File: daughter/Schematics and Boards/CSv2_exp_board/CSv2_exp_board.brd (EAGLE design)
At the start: 38.1 x 43.8 mm, 133 parts, among them J1 HIROSE-DF40_44-PIN_CONNECTORS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, J2 J-SERIAL-PORT, J3 CORTEX_DEBUG_SMD, J301 HIROSE-DF40_44-PIN_CONNECTORS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, J4 SJ-43514-SMT, J7 J-USB-HIROSE-MICRO-USB, SW1 SPST_TACT-KMR2, SW2 SPST_TACT-KMR2, U1 LOADSWITCH-MIC94164, U10 LOADSWITCH-MIC94164, U11 BMI160, U12 TLV320DAC26IRHB, U13 ADG839YKSZ-500RL7KS_6_ADI-L, U14 LOADSWITCH-MIC94164, U2 ADA4841-1YRJZ-R7, U205 MPL3115A2, U3 Value, U4 RFM69HCW, U5 Value, U6 Value, U7 LOADSWITCH-MIC94164, U8 LOADSWITCH-MIC94164, U9 LOADSWITCH-MIC94164, X1 32.768kHz, X2 32.768, X3 uFL, X4 uFL, X5 uFL, X6 uFL

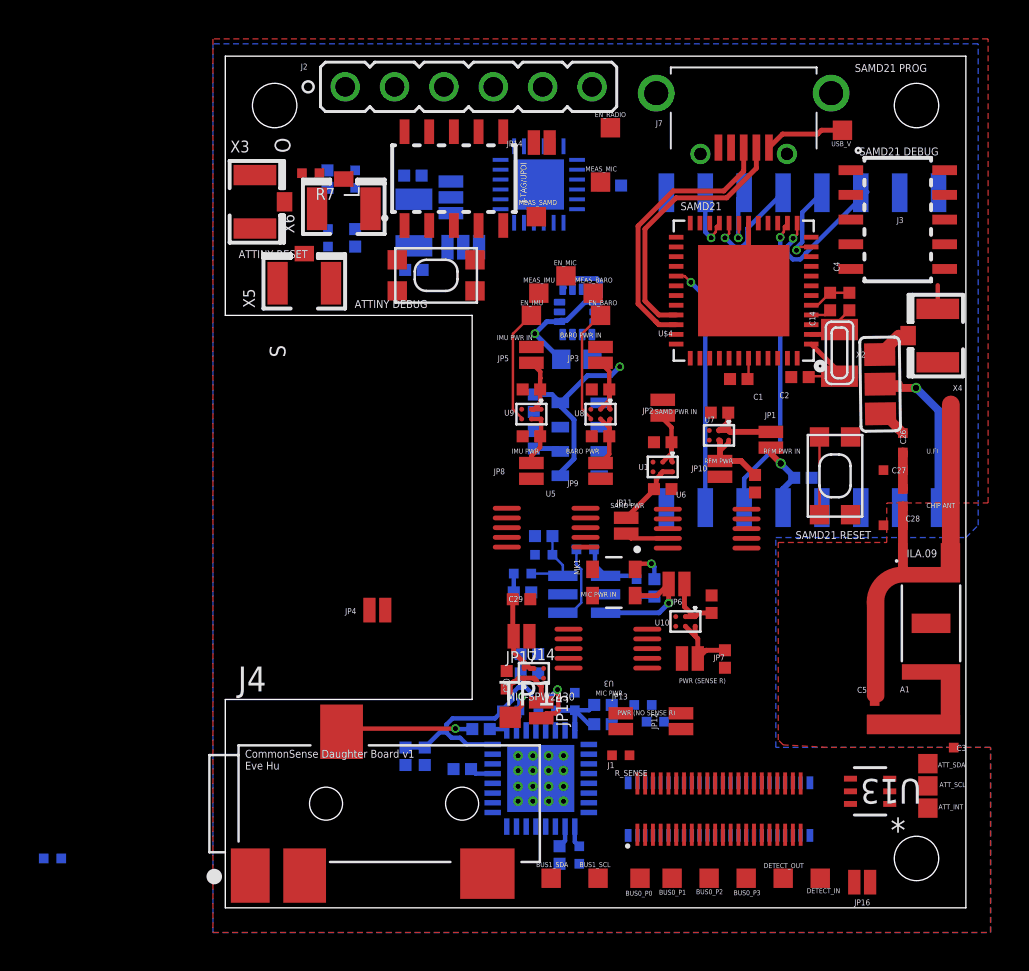
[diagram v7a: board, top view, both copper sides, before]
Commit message: DTR-placement + manual routing
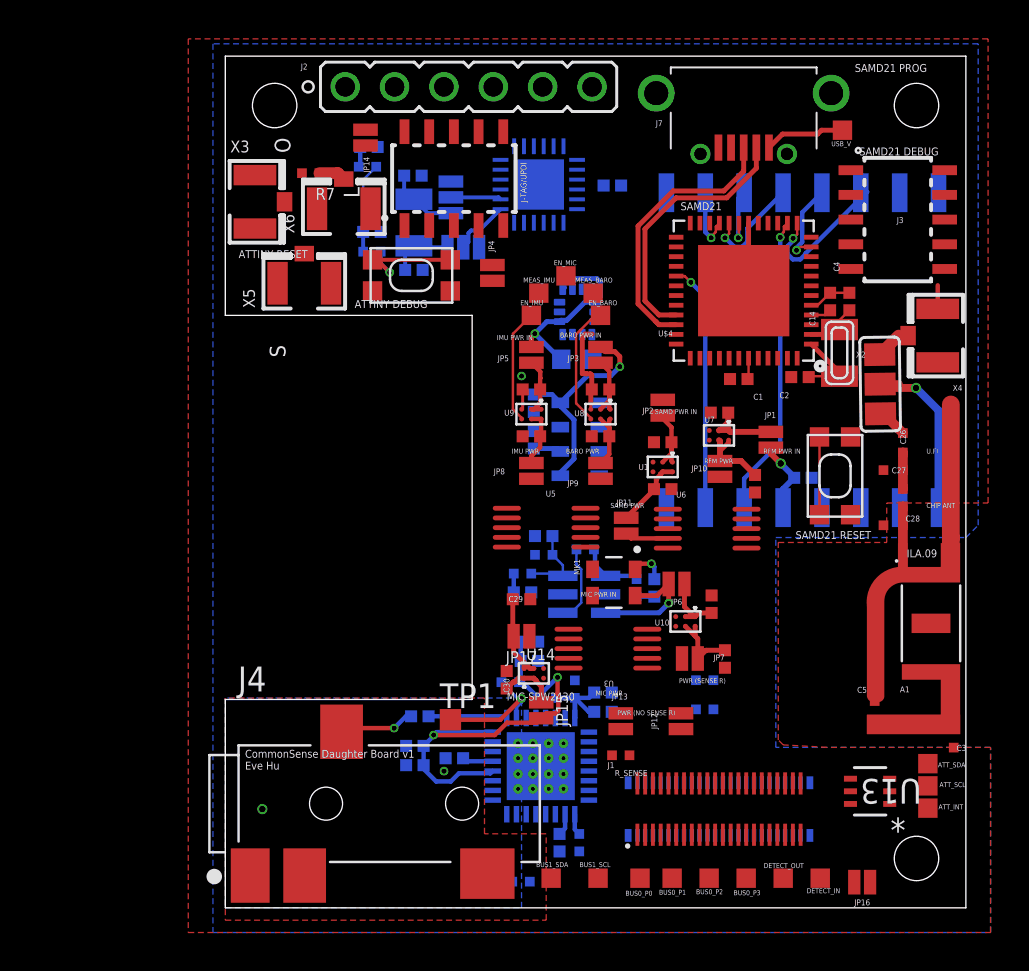
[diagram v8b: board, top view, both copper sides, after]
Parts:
- removed EN_RADIO, MEAS_MIC, MEAS_SAMD: TPTP10SQ, TestPoints:TP10SQ
- moved R12 24.1 mm to (15.2, 1.35), turned to 180 degrees
- moved JP4 18.3 mm to (13.7, 32.7), turned to 90 degrees
- moved JP14 9.07 mm to (7.21, 39.6), turned to 270 degrees
- moved R5 3.42 mm to (24.7, 11.7)
- moved C32 3.22 mm to (10.0, 9.86)
- moved TP1 3.08 mm to (11.6, 9.68)
- moved C12 2.70 mm to (7.39, 39.1), turned to 0 degrees
- moved R6 2.62 mm to (24.7, 10.2)
- moved R3-39R 2.37 mm to (7.54, 33.8), turned to 0 degrees
- moved R11 1.45 mm to (14.7, 11.6), turned to 180 degrees
- moved SW1 1.27 mm to (9.58, 32.5)
- moved C3-4.7N 0.92 mm to (7.54, 34.8), turned to 0 degrees
- moved R1-100K 0.90 mm to (7.32, 38.1), turned to 0 degrees
- moved C37 0.72 mm to (9.75, 8.33), turned to 0 degrees
- moved C31 0.69 mm to (11.8, 7.70)
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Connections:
- net EN_RADIO: no longer EN_RADIO.TP
- net GND: now also U12.V, U12.V_1, U12.V_10, U12.V_11, U12.V_12, U12.V_13, U12.V_14, U12.V_15, U12.V_2, U12.V_3, U12.V_4, U12.V_5, U12.V_6, U12.V_7, U12.V_8, U12.V_9
- net MEAS_MIC: no longer MEAS_MIC.TP
- net MEAS_SAMD: no longer MEAS_SAMD.TP
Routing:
- net N$12: track 0.00 -> 6.41 mm, vias 0 -> 1
- net GND: track 26.5 -> 32.3 mm, vias 0 -> 1
- net +3V3_CODEC: track 17.6 -> 22.8 mm, vias 1 -> 2
- net AT_RESET: track 0.00 -> 4.65 mm
- net N$23: track 0.00 -> 3.62 mm
- net CODEC_!RESET: track 3.18 -> 6.60 mm
- net N$22: track 0.00 -> 3.18 mm
- net N$25: track 0.90 -> 4.06 mm
- net N$18: track 0.00 -> 3.00 mm
- net N$16: track 6.80 -> 3.90 mm
- net N$19: track 0.00 -> 2.59 mm
- net +3V3_BARO: track 9.70 -> 11.4 mm
- net N$11: track 0.00 -> 1.38 mm
- net +3V3_ATT: track 0.00 -> 1.05 mm
- net +3V3_IMU: track 9.23 -> 9.99 mm
- added copper zone on layer 1, net AGND
- added copper zone on layer 16, net AGND
- added copper zone on layer 2, net T
